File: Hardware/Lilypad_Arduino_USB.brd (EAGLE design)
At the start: 50.8 x 50.8 mm, 46 parts, among them U1 MCP73831, U2 MIC5219, U3 ATMEGA32U41:1, Y1 8MHz

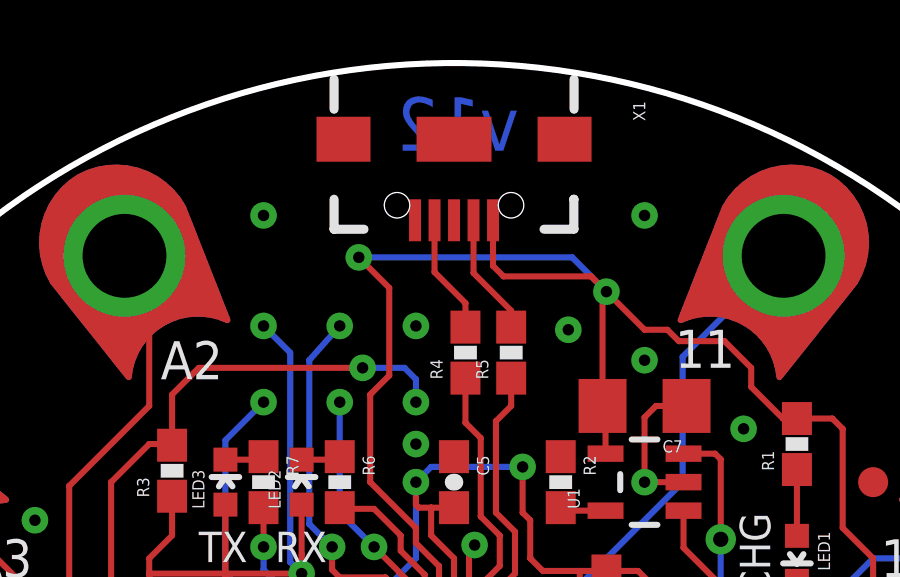
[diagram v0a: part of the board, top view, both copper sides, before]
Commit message: Fixing D+ trace connection
ID line on USB connector was routed to D+ on micro and D+ on USB
connector was unrouted. Fixed now.
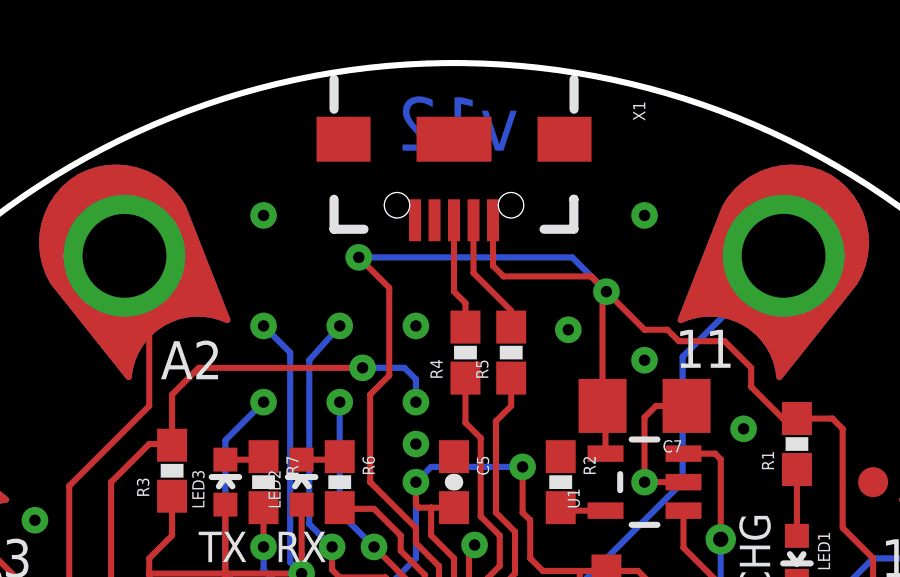
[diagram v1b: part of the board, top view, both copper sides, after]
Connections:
- removed net N$22: X1.D+1
- net N$20: now also X1.D+1; no longer X1.ID1
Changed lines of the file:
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@@
 <signal name="N$20">
 <contactref element="R4" pad="2"/>
-<contactref element="X1" pad="ID1"/>
+<contactref element="X1" pad="D+1"/>
 <wire x1="0.381" y1="16.597996875" x2="0.381" y2="17.399" width="0.2032" layer="1"/>
-<wire x1="-0.649996875" y1="20.16" x2="-0.649996875" y2="18.429996875" width="0.2032" layer="1"/>
-<wire x1="-0.649996875" y1="18.429996875" x2="0.381" y2="17.399" width="0.2032" layer="1"/>
+<wire x1="0.381" y1="17.399" x2="0" y2="17.78" width="0.2032" layer="1"/>
+<wire x1="0" y1="17.78" x2="0" y2="20.159996875" width="0.2032" layer="1"/>
+<wire x1="0" y1="20.159996875" x2="0.000003125" y2="20.16" width="0.2032" layer="1"/>
 </signal>
 <signal name="D+">
@@
 <wire x1="5.08000625" y1="-2.909" x2="4.203" y2="-2.909" width="0.2032" layer="1"/>
 </signal>
-<signal name="N$22">
-<contactref element="X1" pad="D+1"/>
-</signal>
 </signals>
